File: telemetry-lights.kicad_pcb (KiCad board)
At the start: 2 copper layers, 29 parts, among them J1 CONN HEADER VERT 3POS 2.5MM, J2 CONN HEADER VERT 4POS 2.5MM, J5 PIN HEADER 2.54MM PITCH STR D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, J6 CONN HEADER VERT 2POS 1.5MM, J7 CONN HEADER VERT 2POS 1.5MM, U2 STM32L431KBU6TR, U3 IAM-20381HT

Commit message: Component Placement Complete - To be Verified and Traced
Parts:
- moved J7 80.3 mm to (78.5, 95.5), turned to 180 degrees
- moved J6 78.4 mm to (78.2, 113.2), turned to 180 degrees
- moved J1 77.5 mm to (85.2, 111.5), turned to 180 degrees
- moved BOOT1 76.6 mm to (86.0, 99.0)
- moved C27 70.8 mm to (77.5, 108.2), turned to 180 degrees
- moved C26 70.5 mm to (77.5, 101.2), turned to 180 degrees
- moved R3 69.5 mm to (83.2, 107.2)
- moved R2 69.4 mm to (82.7, 99.0), turned to 180 degrees
- moved SDA1 68.4 mm to (94.0, 107.8), turned to 180 degrees
- moved SCL1 68.4 mm to (94.0, 104.8), turned to 180 degrees
- moved C16 67.1 mm to (77.5, 103.0), turned to 180 degrees
- moved C17 67.0 mm to (77.5, 104.8), turned to 180 degrees
- moved C22 66.9 mm to (77.5, 99.5), turned to 180 degrees
- moved C18 66.9 mm to (77.5, 106.5), turned to 180 degrees
- moved R1 66.0 mm to (82.8, 97.2)
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
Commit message: started tracing
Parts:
- moved C27 8.75 mm to (77.5, 99.5)
- moved R5 2.00 mm to (89.0, 108.0), turned to 0 degrees
- moved R6 1.75 mm to (89.0, 106.0), turned to 0 degrees
- moved C16 1.75 mm to (77.5, 104.8)
- moved C17 1.75 mm to (77.5, 106.5)
- moved C18 1.75 mm to (77.5, 108.2)
- moved C22 1.75 mm to (77.5, 101.2)
- moved C26 1.75 mm to (77.5, 103.0)
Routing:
- net /SDA: track 0.00 -> 21.0 mm
- net Net-(J1-Pad2): track 0.00 -> 7.24 mm
- net /SCL: track 0.00 -> 5.66 mm
- net /LIGHT: track 0.00 -> 1.93 mm
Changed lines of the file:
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@@
 	(footprint "Capacitor_SMD:C_0603_1608Metric"
 		(layer "F.Cu")
-		(at 77.5 104.75 180)
+		(at 77.5 106.5 180)
 		(descr "Capacitor SMD 0603 (1608 Metric), square (rectangular) end terminal, IPC-7351 nominal, (Body size source: IPC-SM-782 page 76, https://www.pcb-3d.com/wordpress/wp-content/uploads/ipc-sm-782a_amendment_1_and_2.pdf)")
 		(tags "capacitor")
@@
 	(footprint "Capacitor_SMD:C_0603_1608Metric"
 		(layer "F.Cu")
-		(at 77.5 108.25 180)
+		(at 77.5 99.5 180)
 		(descr "Capacitor SMD 0603 (1608 Metric), square (rectangular) end terminal, IPC-7351 nominal, (Body size source: IPC-SM-782 page 76, https://www.pcb-3d.com/wordpress/wp-content/uploads/ipc-sm-782a_amendment_1_and_2.pdf)")
 		(tags "capacitor")
@@
 		)
 		(embedded_fonts no)
-		(model "${KICAD6_3DMODEL_DIR}/Diode_SMD.3dshapes/D_SOD-323F.wrl"
+		(model "${KICAD10_3DMODEL_DIR}/Diode_SMD.3dshapes/D_SOD-323F.step"
 			(hide yes)
 			(offset
@@
 	(footprint "Resistor_SMD:R_0603_1608Metric_Pad0.98x0.95mm_HandSolder"
 		(layer "F.Cu")
-		(at 89.000001 106 180)
+		(at 89 108)
 		(descr "Resistor SMD 0603 (1608 Metric), square (rectangular) end terminal, IPC-7351 nominal with elongated pad for handsoldering. (Body size source: IPC-SM-782 page 72, https://www.pcb-3d.com/wordpress/wp-content/uploads/ipc-sm-782a_amendment_1_and_2.pdf)")
 		(tags "resistor handsolder")
@@
 		(duplicate_pad_numbers_are_jumpers no)
 		(fp_line
-			(start -0.254724 0.5225)
-			(end 0.254724 0.5225)
+			(start -0.254724 -0.5225)
+			(end 0.254724 -0.5225)
 			(stroke
 				(width 0.12)
@@
 		)
 		(fp_line
-			(start -0.254724 -0.5225)
-			(end 0.254724 -0.5225)
+			(start -0.254724 0.5225)
+			(end 0.254724 0.5225)
 			(stroke
 				(width 0.12)
@@
 		)
 		(pad "1" smd roundrect
-			(at -0.9125 0 180)
+			(at -0.9125 0)
 			(size 0.975 0.95)
 			(layers "F.Cu" "F.Mask" "F.Paste")
@@
 		)
 		(pad "2" smd roundrect
-			(at 0.9125 0 180)
+			(at 0.9125 0)
 			(size 0.975 0.95)
 			(layers "F.Cu" "F.Mask" "F.Paste")
@@
 	(footprint "Capacitor_SMD:C_0603_1608Metric"
 		(layer "F.Cu")
-		(at 77.5 103 180)
+		(at 77.5 104.75 180)
 		(descr "Capacitor SMD 0603 (1608 Metric), square (rectangular) end terminal, IPC-7351 nominal, (Body size source: IPC-SM-782 page 76, https://www.pcb-3d.com/wordpress/wp-content/uploads/ipc-sm-782a_amendment_1_and_2.pdf)")
 		(tags "capacitor")
@@
 	(footprint "Capacitor_SMD:C_0603_1608Metric"
 		(layer "F.Cu")
-		(at 77.5 99.5 180)
+		(at 77.5 101.25 180)
 		(descr "Capacitor SMD 0603 (1608 Metric), square (rectangular) end terminal, IPC-7351 nominal, (Body size source: IPC-SM-782 page 76, https://www.pcb-3d.com/wordpress/wp-content/uploads/ipc-sm-782a_amendment_1_and_2.pdf)")
 		(tags "capacitor")
@@
 	(footprint "Capacitor_SMD:C_0603_1608Metric"
 		(layer "F.Cu")
-		(at 77.5 101.25 180)
+		(at 77.5 103 180)
 		(descr "Capacitor SMD 0603 (1608 Metric), square (rectangular) end terminal, IPC-7351 nominal, (Body size source: IPC-SM-782 page 76, https://www.pcb-3d.com/wordpress/wp-content/uploads/ipc-sm-782a_amendment_1_and_2.pdf)")
 		(tags "capacitor")
@@
 	(footprint "Capacitor_SMD:C_0603_1608Metric"
 		(layer "F.Cu")
-		(at 77.5 106.5 180)
+		(at 77.5 108.25 180)
 		(descr "Capacitor SMD 0603 (1608 Metric), square (rectangular) end terminal, IPC-7351 nominal, (Body size source: IPC-SM-782 page 76, https://www.pcb-3d.com/wordpress/wp-content/uploads/ipc-sm-782a_amendment_1_and_2.pdf)")
 		(tags "capacitor")
@@
 	(footprint "Resistor_SMD:R_0603_1608Metric_Pad0.98x0.95mm_HandSolder"
 		(layer "F.Cu")
-		(at 89.000001 107.75 180)
+		(at 89 106)
 		(descr "Resistor SMD 0603 (1608 Metric), square (rectangular) end terminal, IPC-7351 nominal with elongated pad for handsoldering. (Body size source: IPC-SM-782 page 72, https://www.pcb-3d.com/wordpress/wp-content/uploads/ipc-sm-782a_amendment_1_and_2.pdf)")
 		(tags "resistor handsolder")
@@
 		(duplicate_pad_numbers_are_jumpers no)
 		(fp_line
-			(start -0.254724 0.5225)
-			(end 0.254724 0.5225)
+			(start -0.254724 -0.5225)
+			(end 0.254724 -0.5225)
 			(stroke
 				(width 0.12)
@@
 		)
 		(fp_line
-			(start -0.254724 -0.5225)
-			(end 0.254724 -0.5225)
+			(start -0.254724 0.5225)
+			(end 0.254724 0.5225)
 			(stroke
 				(width 0.12)
@@
 		)
 		(pad "1" smd roundrect
-			(at -0.9125 0 180)
+			(at -0.9125 0)
 			(size 0.975 0.95)
 			(layers "F.Cu" "F.Mask" "F.Paste")
@@
 		)
 		(pad "2" smd roundrect
-			(at 0.9125 0 180)
+			(at 0.9125 0)
 			(size 0.975 0.95)
 			(layers "F.Cu" "F.Mask" "F.Paste")
@@
 		)
 	)
+	(segment
+		(start 78.5 99.275)
+		(end 78.275 99.5)
+		(width 0.2)
+		(layer "F.Cu")
+		(net "3V3")
+	)
+	(segment
+		(start 88.0875 108)
+		(end 86.5 106.4125)
+		(width 0.2)
+		(layer "F.Cu")
+		(net "/SCL")
+	)
+	(segment
+		(start 86.250001 103.750001)
+		(end 85.6 103.750001)
+		(width 0.2)
+		(layer "F.Cu")
+		(net "/SCL")
+	)
+	(segment
+		(start 86.5 104)
+		(end 86.250001 103.750001)
+		(width 0.2)
+		(layer "F.Cu")
+		(net "/SCL")
+	)
+	(segment
+		(start 86.5 106.4125)
+		(end 86.5 104)
+		(width 0.2)
+		(layer "F.Cu")
+		(net "/SCL")
+	)
+	(segment
+		(start 90.550001 103.191422)
+		(end 90.550001 101.825)
+		(width 0.2)
+		(layer "F.Cu")
+		(net "/SDA")
+	)
+	(segment
+		(start 93.25 107)
+		(end 94 107.75)
+		(width 0.2)
+		(layer "F.Cu")
+		(net "/SDA")
+	)
+	(segment
+		(start 91.5 107)
+		(end 93.25 107)
+		(width 0.2)
+		(layer "F.Cu")
+		(net "/SDA")
+	)
+	(segment
+		(start 91.5 107)
+		(end 91.5 104.141421)
+		(width 0.2)
+		(layer "F.Cu")
+		(net "/SDA")
+	)
+	(segment
+		(start 86.75 103.25)
+		(end 85.6 103.25)
+		(width 0.2)
+		(layer "F.Cu")
+		(net "/SDA")
+	)
+	(segment
+		(start 91.5 104.141421)
+		(end 90.550001 103.191422)
+		(width 0.2)
+		(layer "F.Cu")
+		(net "/SDA")
+	)
+	(segment
+		(start 87 103.5)
+		(end 86.75 103.25)
+		(width 0.2)
+		(layer "F.Cu")
+		(net "/SDA")
+	)
+	(segment
+		(start 87 104.9125)
+		(end 87 103.5)
+		(width 0.2)
+		(layer "F.Cu")
+		(net "/SDA")
+	)
+	(segment
+		(start 89.0875 107)
+		(end 91.5 107)
+		(width 0.2)
+		(layer "F.Cu")
+		(net "/SDA")
+	)
+	(segment
+		(start 90.625001 101.75)
+		(end 91.025001 101.75)
+		(width 0.2)
+		(layer "F.Cu")
+		(net "/SDA")
+	)
+	(segment
+		(start 90.550001 101.825)
+		(end 90.625001 101.75)
+		(width 0.2)
+		(layer "F.Cu")
+		(net "/SDA")
+	)
+	(segment
+		(start 94.25 107.5)
+		(end 94 107.75)
+		(width 0.2)
+		(layer "F.Cu")
+		(net "/SDA")
+	)
+	(segment
+		(start 88.0875 106)
+		(end 87 104.9125)
+		(width 0.2)
+		(layer "F.Cu")
+		(net "/SDA")
+	)
+	(segment
+		(start 97.75 107.5)
+		(end 94.25 107.5)
+		(width 0.2)
+		(layer "F.Cu")
+		(net "/SDA")
+	)
+	(segment
+		(start 88.0875 106)
+		(end 89.0875 107)
+		(width 0.2)
+		(layer "F.Cu")
+		(net "/SDA")
+	)
+	(segment
+		(start 82.499999 105.35)
+		(end 82.499999 107.175001)
+		(width 0.25)
+		(layer "F.Cu")
+		(net "/LIGHT")
+	)
+	(segment
+		(start 82.499999 107.175001)
+		(end 82.425 107.25)
+		(width 0.2)
+		(layer "F.Cu")
+		(net "/LIGHT")
+	)
+	(segment
+		(start 87 109.5)
+		(end 87.75 110.25)
+		(width 0.25)
+		(layer "F.Cu")
+		(net "Net-(J1-Pad2)")
+	)
+	(segment
+		(start 87.75 110.25)
+		(end 87.75 111.5)
+		(width 0.25)
+		(layer "F.Cu")
+		(net "Net-(J1-Pad2)")
+	)
+	(segment
+		(start 84.5 109.5)
+		(end 87 109.5)
+		(width 0.25)
+		(layer "F.Cu")
+		(net "Net-(J1-Pad2)")
+	)
+	(segment
+		(start 84.075 107.25)
+		(end 84.075 109.075)
+		(width 0.25)
+		(layer "F.Cu")
+		(net "Net-(J1-Pad2)")
+	)
+	(segment
+		(start 84.075 109.075)
+		(end 84.5 109.5)
+		(width 0.25)
+		(layer "F.Cu")
+		(net "Net-(J1-Pad2)")
+	)
 	(embedded_fonts no)

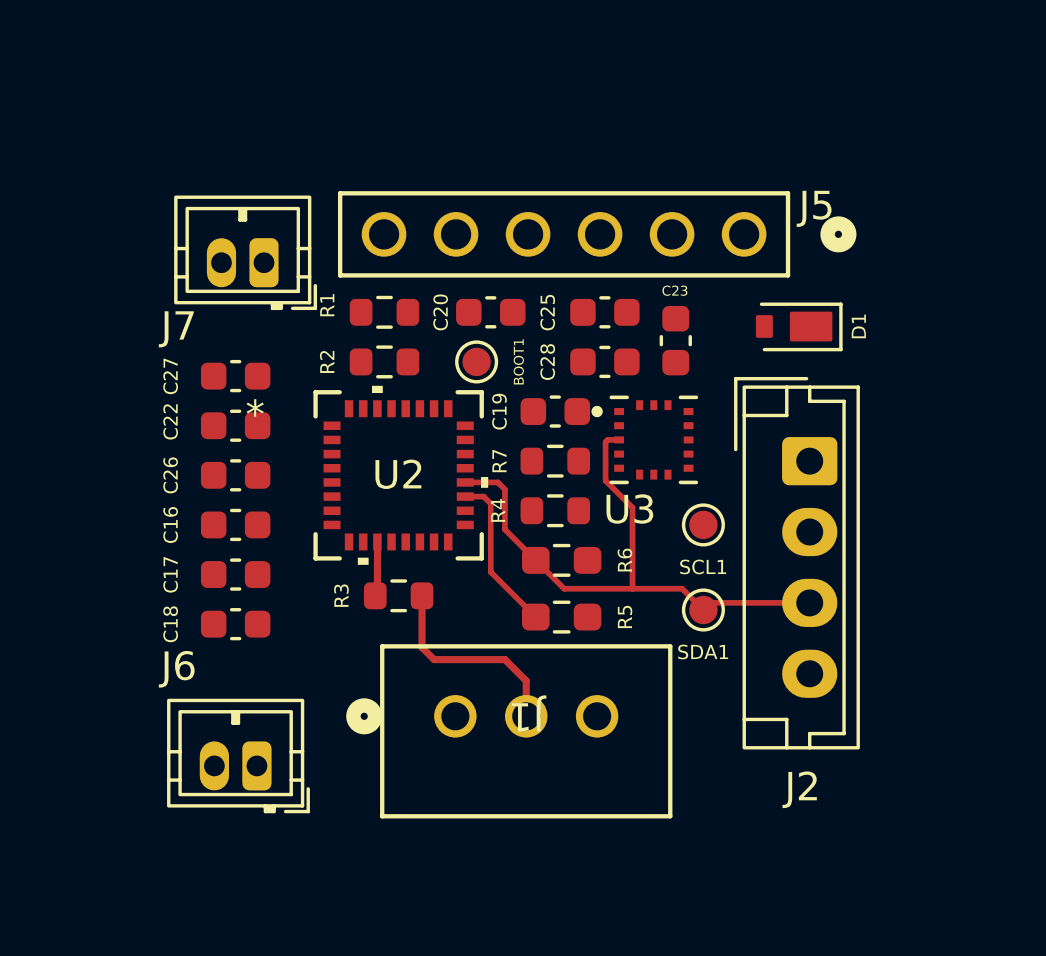
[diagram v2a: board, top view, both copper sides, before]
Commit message: Add connections and copper fill
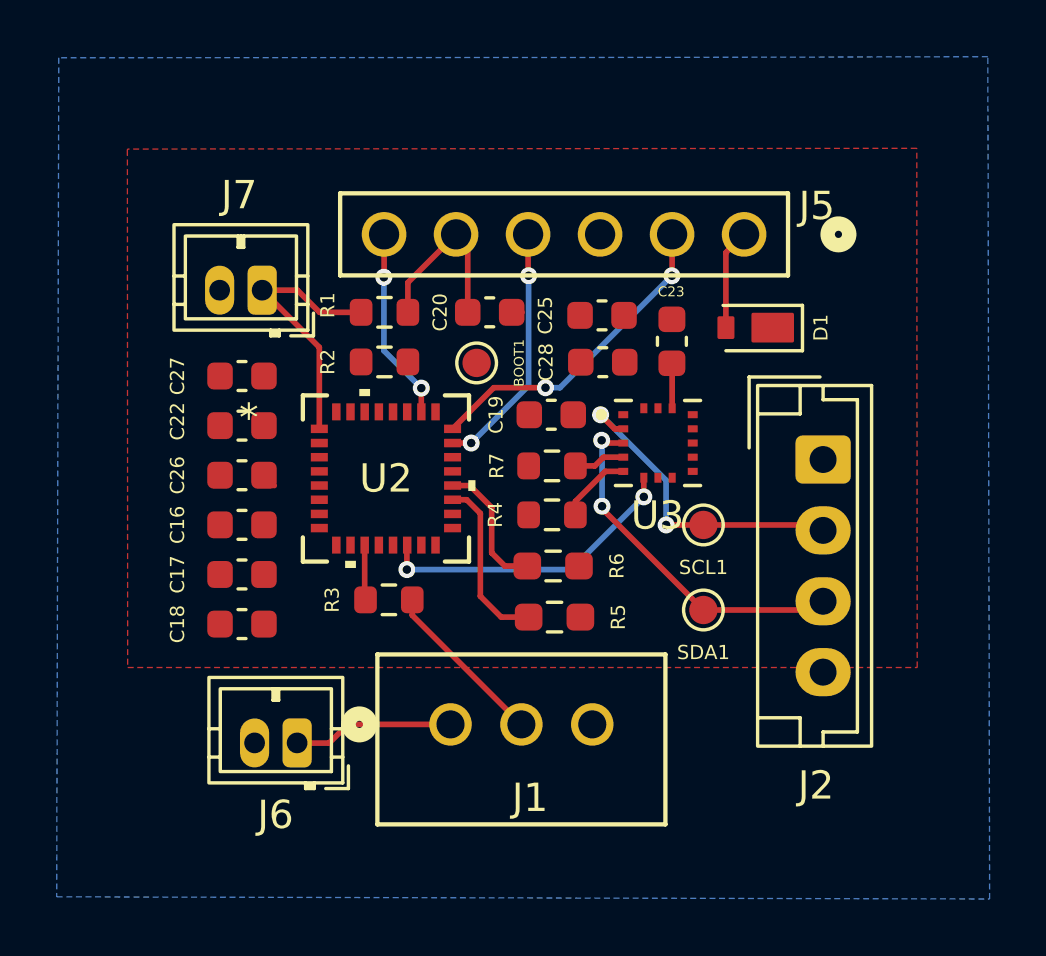
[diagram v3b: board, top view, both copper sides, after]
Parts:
- moved J6 1.63 mm to (79.7, 112.4)
- moved D1 1.36 mm to (96.4, 97.8)
- moved J7 0.97 mm to (78.4, 96.5)
- moved J2 0.48 mm to (98.2, 102.4)
- moved U2 0.46 mm to (82.8, 103.1)
- moved R3 0.37 mm to (82.9, 107.4)
- moved R6 0.36 mm to (88.7, 106.2)
- moved J1 0.33 mm to (85.1, 111.8)
- moved R5 0.25 mm to (88.7, 108.0)
- moved C16 0.22 mm to (77.7, 104.7)
- moved C17 0.22 mm to (77.7, 106.5)
- moved C18 0.22 mm to (77.7, 108.2)
- moved C22 0.22 mm to (77.7, 101.2)
- moved C26 0.22 mm to (77.7, 103.0)
- moved C27 0.22 mm to (77.7, 99.5)
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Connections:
- U2 pad 14: unconnected-(U2A-PB0-Pad14) -> /WAKE
- U2 pad 23: unconnected-(U2A-PA13-Pad23) -> /SWDIO
- U2 pad 24: unconnected-(U2A-PA14-Pad24) -> /SWCLK
- U2 pad 26: unconnected-(U2A-PB3-Pad26) -> /SWO
- U2 pad 6: /WAKE -> unconnected-(U2A-PA0/CK_IN-Pad6)
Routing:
- net /SCL: track 5.66 -> 17.6 mm, vias 0 -> 2
- net /SWCLK: track 0.00 -> 11.4 mm, vias 0 -> 2
- net /WAKE: track 0.00 -> 11.0 mm, vias 0 -> 2
- net 3V3: track 0.32 -> 10.4 mm
- net /SWDIO: track 0.00 -> 8.86 mm, vias 0 -> 2
- net /SWO: track 0.00 -> 6.81 mm, vias 0 -> 2
- net /NRST: track 0.00 -> 6.37 mm
- net 5V: track 0.00 -> 5.69 mm
- net Net-(D1-A): track 0.00 -> 3.56 mm
- net /SDA: track 21.0 -> 17.7 mm, vias 0 -> 2
- net /CS: track 0.00 -> 2.63 mm
- net /SA0: track 0.00 -> 1.82 mm
- net Net-(U3-REGOUT): track 0.00 -> 1.66 mm
- net Net-(J1-Pad2): track 7.24 -> 5.99 mm
- net GND: track 0.00 -> 0.67 mm
- added copper zone on F.Cu, net 3V3
- added copper zone on B.Cu, net GND

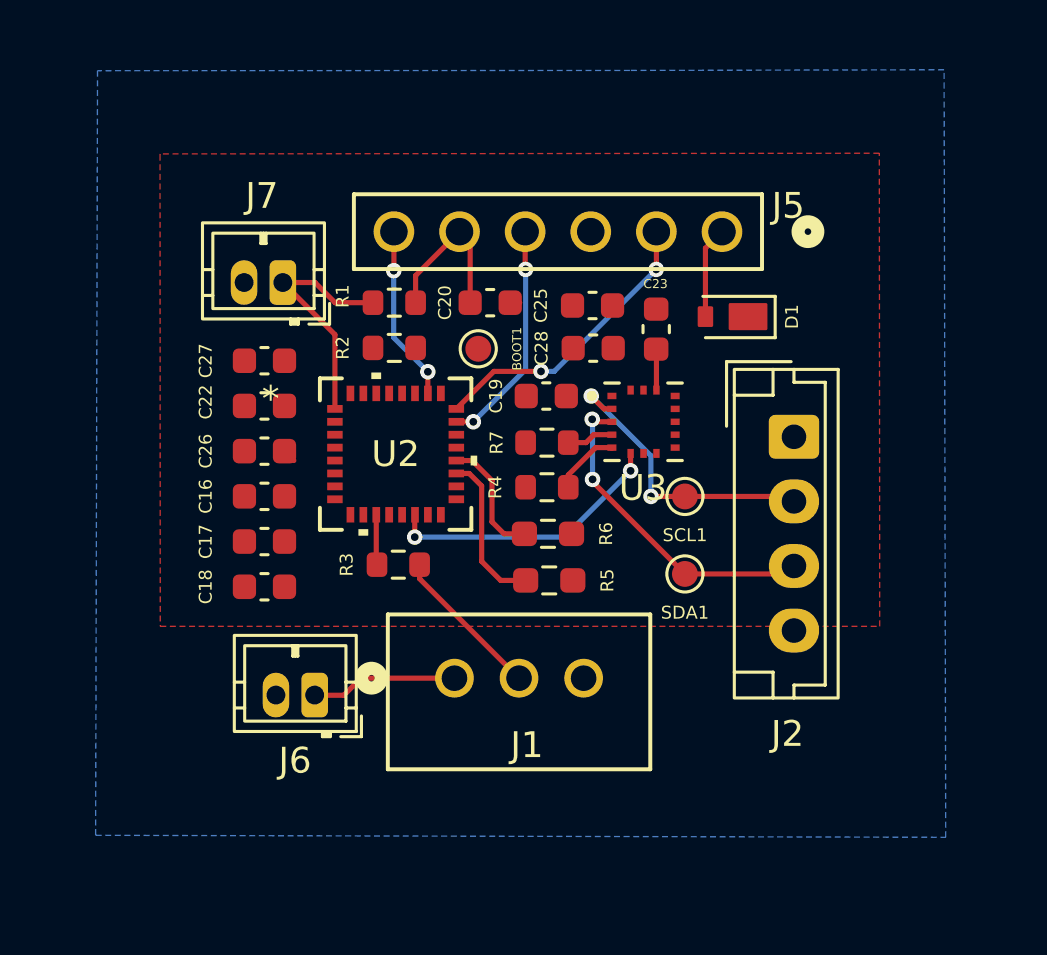
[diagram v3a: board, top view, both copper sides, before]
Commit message: Update trace thickness and fill zones
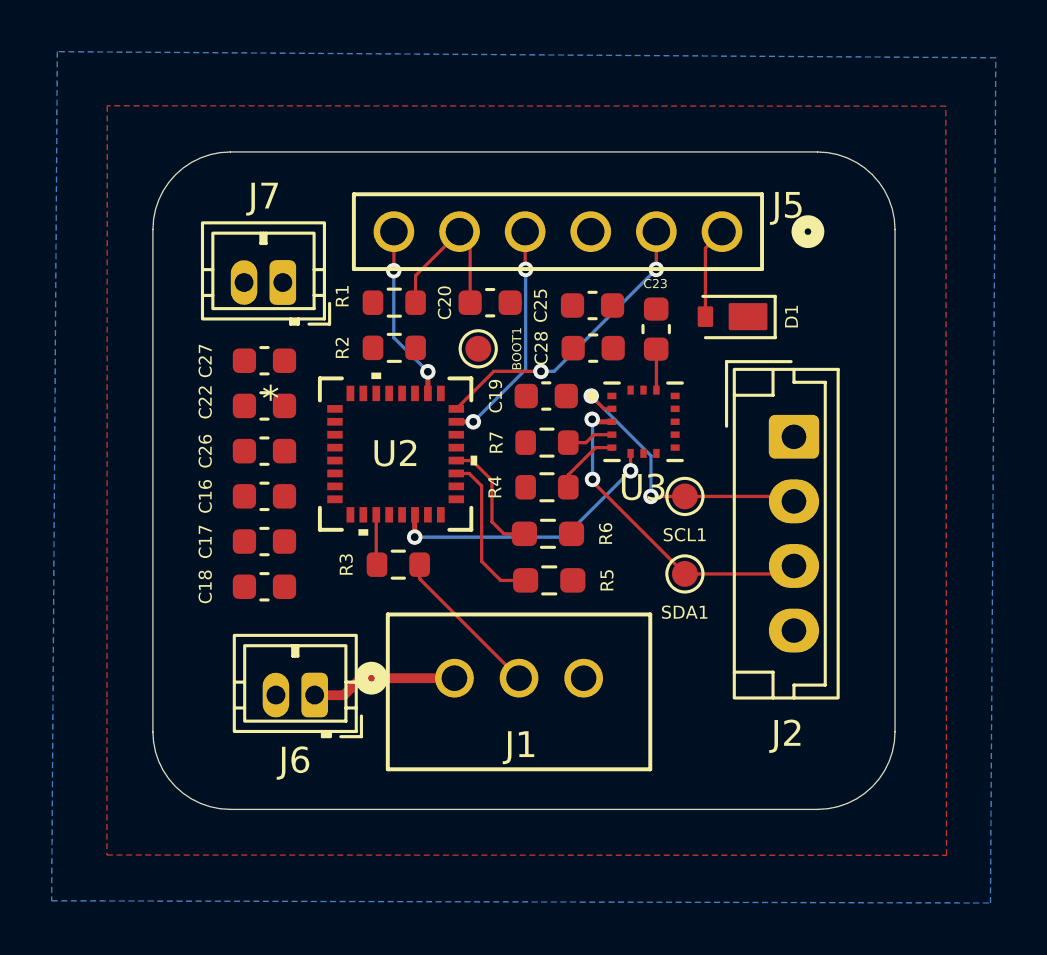
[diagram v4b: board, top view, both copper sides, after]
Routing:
- net 3V3: track 10.4 -> 0.83 mm
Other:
- board outline added: 28.7 x 25.5 mm

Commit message: updated layout
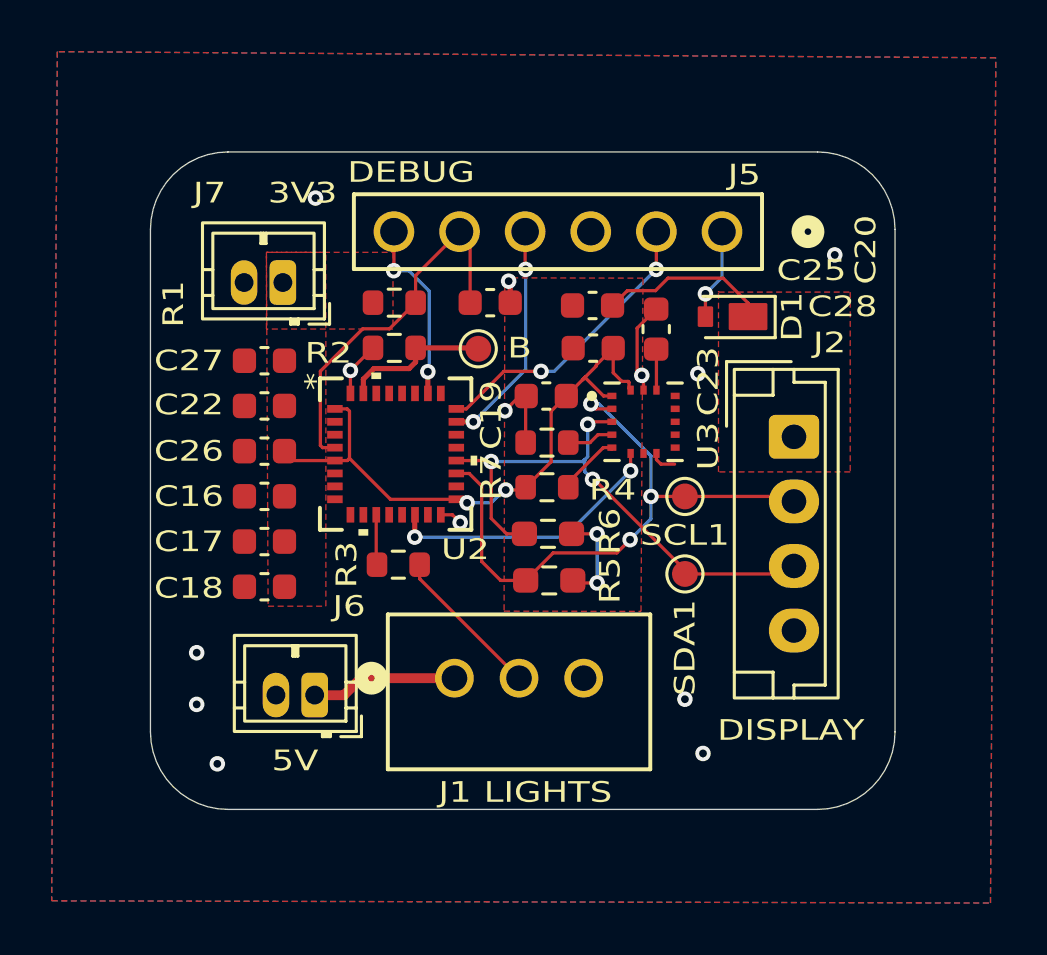
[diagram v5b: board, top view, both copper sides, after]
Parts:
- renumbered J6 to 5V, BOOT1 to B
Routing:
- net 3V3: track 0.83 -> 34.2 mm, vias 0 -> 4
- net GND: track 0.67 -> 11.6 mm, vias 0 -> 13
- net /NRST: track 6.37 -> 14.6 mm
- net /SCL: track 17.6 -> 24.1 mm, vias 2 -> 3
- net Net-(U2A-PH3/BOOT0): track 0.00 -> 5.84 mm
- net /SDA: track 17.7 -> 22.1 mm, vias 2 -> 3
- net Net-(D1-A): vias 0 -> 1
- added copper zone on F.Cu, net GND
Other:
- board size 28.7 x 25.5 mm -> 28.8 x 25.5 mm
- board text added: "3V3"
- board text added: "DEBUG"
- board text added: "DISPLAY"
- board text added: "J6"
- board text added: "LIGHTS"
